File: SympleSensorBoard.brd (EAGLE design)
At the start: 50.8 x 50.8 mm, 49 parts, among them IC1 STM32F303K8T6, J1 B2B-XH-A_LF__SN_, J10 B3B-XH-A_LF__SN_, J11 B3B-XH-A_LF__SN_, J12 B4B-XH-A_LF__SN_, J13 B4B-XH-A_LF__SN_, J14 B4B-XH-A_LF__SN_, J15 B4B-XH-A_LF__SN_, J16 B2B-XH-A_LF__SN_, J2 B2B-XH-A_LF__SN_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

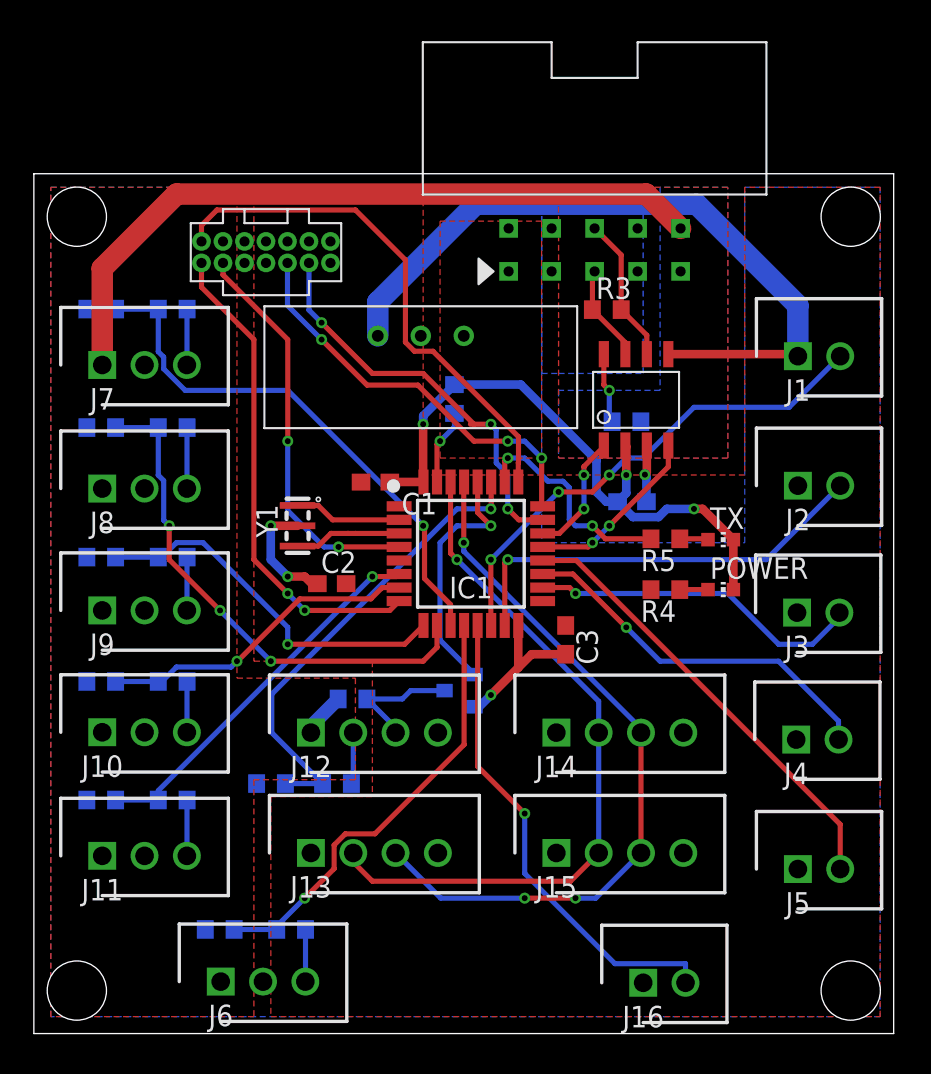
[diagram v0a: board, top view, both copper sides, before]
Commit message: コネクタ位置の修正、コネクタ番号を基盤上に表示、部品の再配置、再配線完了。使うセンサはまだ決まっていない。
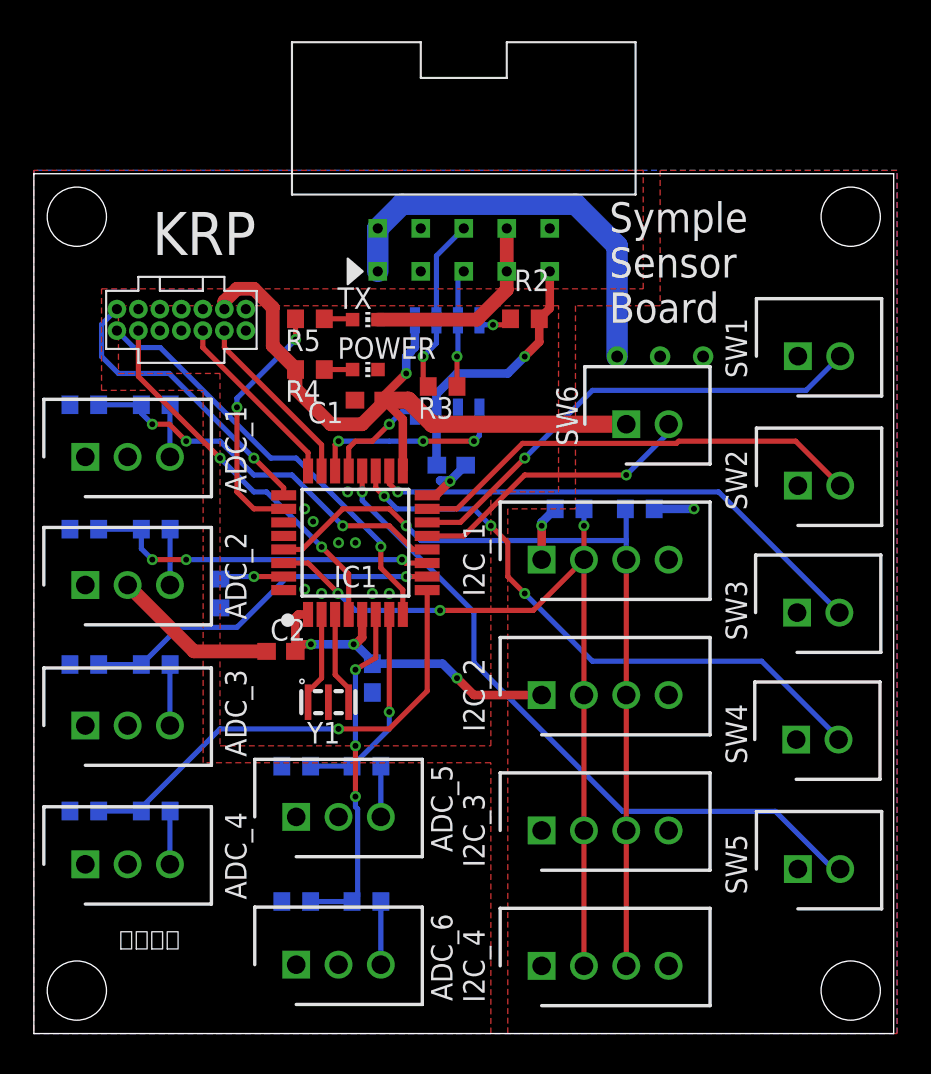
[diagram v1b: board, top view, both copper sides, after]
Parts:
- removed J10, J11, J6, J7, J8, J9: B3B-XH-A_LF__SN_, B3B-XH-A_LF__SN_:SHDR3W64P0X250_1X3_990X575X700
- removed J12, J13, J14, J15: B4B-XH-A_LF__SN_, B4B-XH-A_LF__SN_:SHDR4W64P0X250_1X4_1240X575X70
- removed J16: B2B-XH-A_LF__SN_, B2B-XH-A_LF__SN_:SHDR2W64P0X250_1X2_740X575X700
- removed MOSFET1: IRLML6344TRPBFTR, mukuchin_transistor_fet_igbt:IRLML6344TRPBF
- removed R18: 10k, rcl:R0603
- removed R19: 1k, rcl:R0603
- removed R20: 2k, rcl:R0603
- added ADC_1, ADC_2, ADC_3, ADC_4, ADC_5, ADC_6: B3B-XH-A_LF__SN_, B3B-XH-A_LF__SN_:SHDR3W64P0X250_1X3_990X575X700
- added I2C_1, I2C_2, I2C_3, I2C_4: B4B-XH-A_LF__SN_, B4B-XH-A_LF__SN_:SHDR4W64P0X250_1X4_1240X575X70
- added R21, R22: 10k, rcl:R0603
- added SW6: B2B-XH-A_LF__SN_, B2B-XH-A_LF__SN_:SHDR2W64P0X250_1X2_740X575X700
- moved R6 32.0 mm to (7.20, 37.1)
- moved R7 32.0 mm to (2.98, 37.1)
- moved R4 24.7 mm to (16.3, 39.2)
- moved R5 24.7 mm to (16.3, 42.2)
- moved POWER 24.7 mm to (19.6, 39.2)
- moved TX 24.7 mm to (19.6, 42.2)
- moved R1 18.0 mm to (11.0, 26.0), turned to 270 degrees
- moved R12 15.0 mm to (7.20, 13.2)
- moved R13 15.0 mm to (2.98, 13.2)
- moved U$1 14.2 mm to (37.0, 40.0), flipped to the bottom
- moved R10 14.0 mm to (7.20, 21.8)
- moved R11 14.0 mm to (2.98, 21.8)
- moved R8 13.0 mm to (7.20, 29.8)
- moved R9 13.0 mm to (2.98, 29.8)
- moved R17 13.0 mm to (15.5, 7.80)
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- renumbered J1 to SW1, J2 to SW2, J3 to SW3, J4 to SW4, J5 to SW5
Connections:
- removed net ECHO: IC1.28, MOSFET1.P$1
- removed net N$11: J12.3, MOSFET1.P$3, R18.1
- removed net N$13: J12.2, R19.1
- removed net TRIG: IC1.27, R19.2, R20.2
- net +3.3V: now also I2C_1.1, I2C_2.1, I2C_3.1, I2C_4.1, R21.1, R22.1, SW6.1; no longer J13.1, J14.1, J15.1, J16.1
- net +5V: now also ADC_1.1, ADC_2.1, ADC_3.1, ADC_4.1, ADC_5.1, ADC_6.1; no longer J10.1, J11.1, J12.1, J6.1, J7.1, J8.1, J9.1, R18.2
- net GND: now also ADC_1.2, ADC_2.2, ADC_3.2, ADC_4.2, ADC_5.2, ADC_6.2, I2C_1.4, I2C_2.4, I2C_3.4, I2C_4.4; no longer J10.2, J11.2, J12.4, J13.4, J14.4, J15.4, J6.2, J7.2, J8.2, J9.2, MOSFET1.P$2, R20.1
- net MSW6: now also SW6.2; no longer J16.2
- net N$10: now also ADC_6.3; no longer J11.3
- net N$5: now also ADC_1.3; no longer J6.3
- net N$6: now also ADC_2.3; no longer J7.3
- net N$7: now also ADC_3.3; no longer J8.3
- net N$8: now also ADC_4.3; no longer J9.3
- net N$9: now also ADC_5.3; no longer J10.3
- net SCL: now also I2C_1.3, I2C_2.3, I2C_3.3, I2C_4.3, R21.2; no longer J13.3, J14.3, J15.3
- net SDA: now also I2C_1.2, I2C_2.2, I2C_3.2, I2C_4.2, R22.2; no longer J13.2, J14.2, J15.2
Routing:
- net +5V: track 48.6 -> 16.0 mm
- net TRIG: track 27.8 -> 0.00 mm, vias 1 -> 0
- net GND: track 52.9 -> 26.0 mm, vias 6 -> 1
- net +3.3V: track 42.4 -> 67.8 mm, vias 0 -> 6
- net +12V: track 0.00 -> 24.8 mm
- net ECHO: track 15.0 -> 0.00 mm, vias 1 -> 0
- net MSW5: track 26.7 -> 40.7 mm, vias 0 -> 1
- net SWDIO: track 24.3 -> 10.7 mm, vias 3 -> 0
- net MSW4: track 22.2 -> 35.7 mm, vias 1 -> 3
- net VCP_RX: track 31.1 -> 17.6 mm, vias 0 -> 1
- net SWCLK: track 24.1 -> 10.9 mm, vias 3 -> 0
- net MSW6: track 28.6 -> 17.3 mm
- net AD2: track 31.9 -> 20.9 mm, vias 1 -> 3
- net MSW3: track 19.9 -> 30.5 mm
- net AD3: track 30.5 -> 21.6 mm, vias 3 -> 1
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- added copper zone on layer 1, net GND
- removed copper zone on layer 1, net +12V
- removed copper zone on layer 16, net +5V
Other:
- board text added: "KRP"
- board text added: "Symple Sensor Board"
- board text added: "向野晴登"

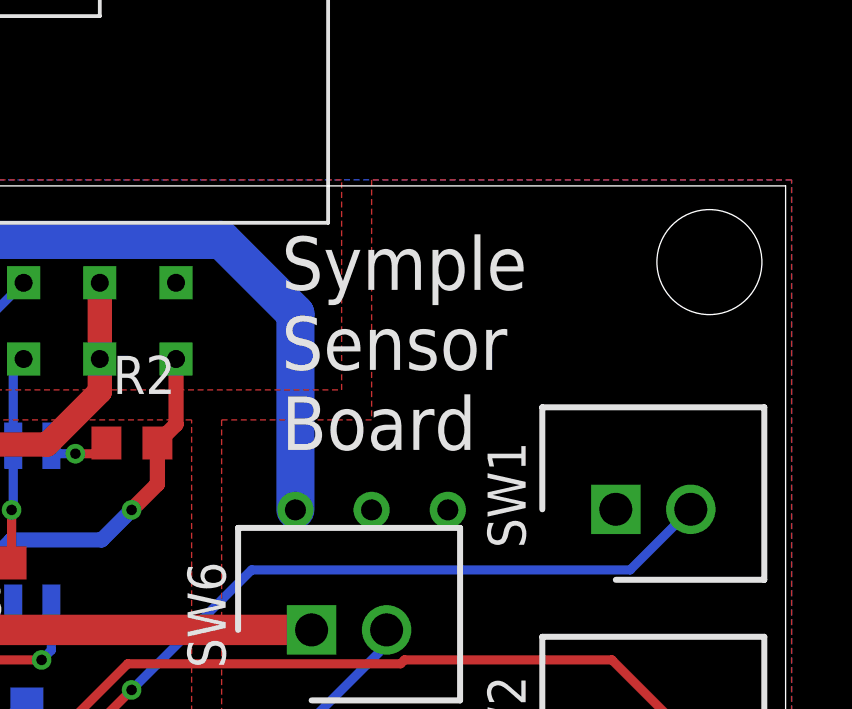
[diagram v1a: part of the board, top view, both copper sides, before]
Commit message: コネクタ位置の修正、コネクタ番号を基盤上に表示、部品の再配置、再配線完了。使うセンサはまだ決まっていない。
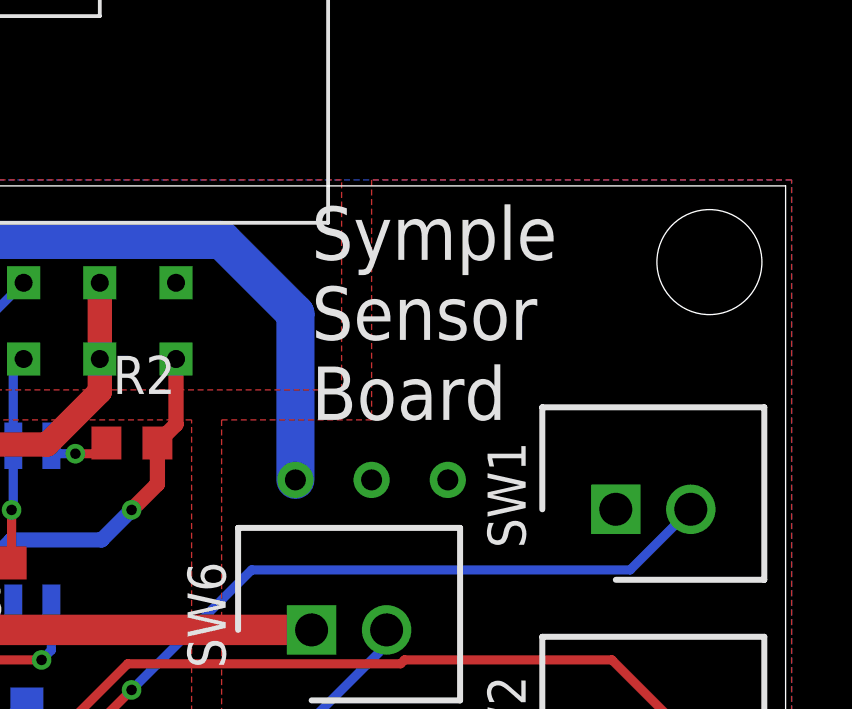
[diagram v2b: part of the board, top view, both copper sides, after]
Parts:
- moved U$1 1.00 mm to (37.0, 41.0)
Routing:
- net +12V: track 24.8 -> 23.8 mm
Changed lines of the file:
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@@
 <hole x="2.54" y="48.26" drill="3.5"/>
 <text x="7" y="46" size="2.54" layer="25">KRP</text>
-<text x="34" y="42" size="1.778" layer="25">Symple
+<text x="35" y="43" size="1.778" layer="25">Symple
 Sensor
 Board</text>
@@
 <attribute name="VALUE" x="31.015" y="32.905" size="1.27" layer="28" rot="MR180"/>
 </element>
-<element name="U$1" library="SympleEncoderBoard" package="DC/DC_REGULATOR_3P" value="BP5293-33" x="37" y="40" smashed="yes" rot="MR180"/>
+<element name="U$1" library="SympleEncoderBoard" package="DC/DC_REGULATOR_3P" value="BP5293-33" x="37" y="41" smashed="yes" rot="MR180"/>
 </elements>
 <signals>
@@
 <wire x1="21.75" y1="49" x2="32" y2="49" width="1.27" layer="16"/>
 <wire x1="32" y1="49" x2="34.46" y2="46.54" width="1.27" layer="16"/>
-<wire x1="34.46" y1="46.54" x2="34.46" y2="40" width="1.27" layer="16"/>
+<wire x1="34.46" y1="46.54" x2="34.46" y2="41" width="1.27" layer="16"/>
 </signal>
 <signal name="+5V">

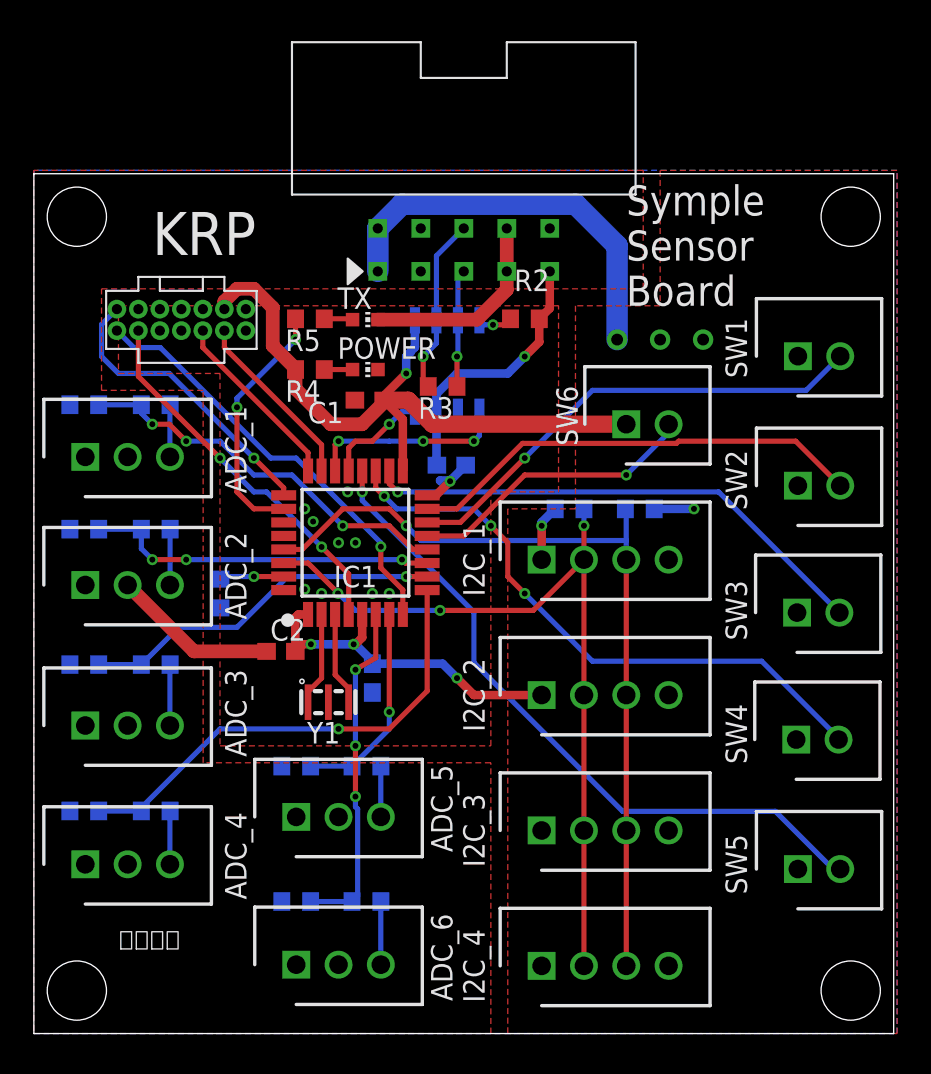
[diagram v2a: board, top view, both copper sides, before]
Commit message: I2Cコネクタを全て外した。I2Cは別の基盤で行う。
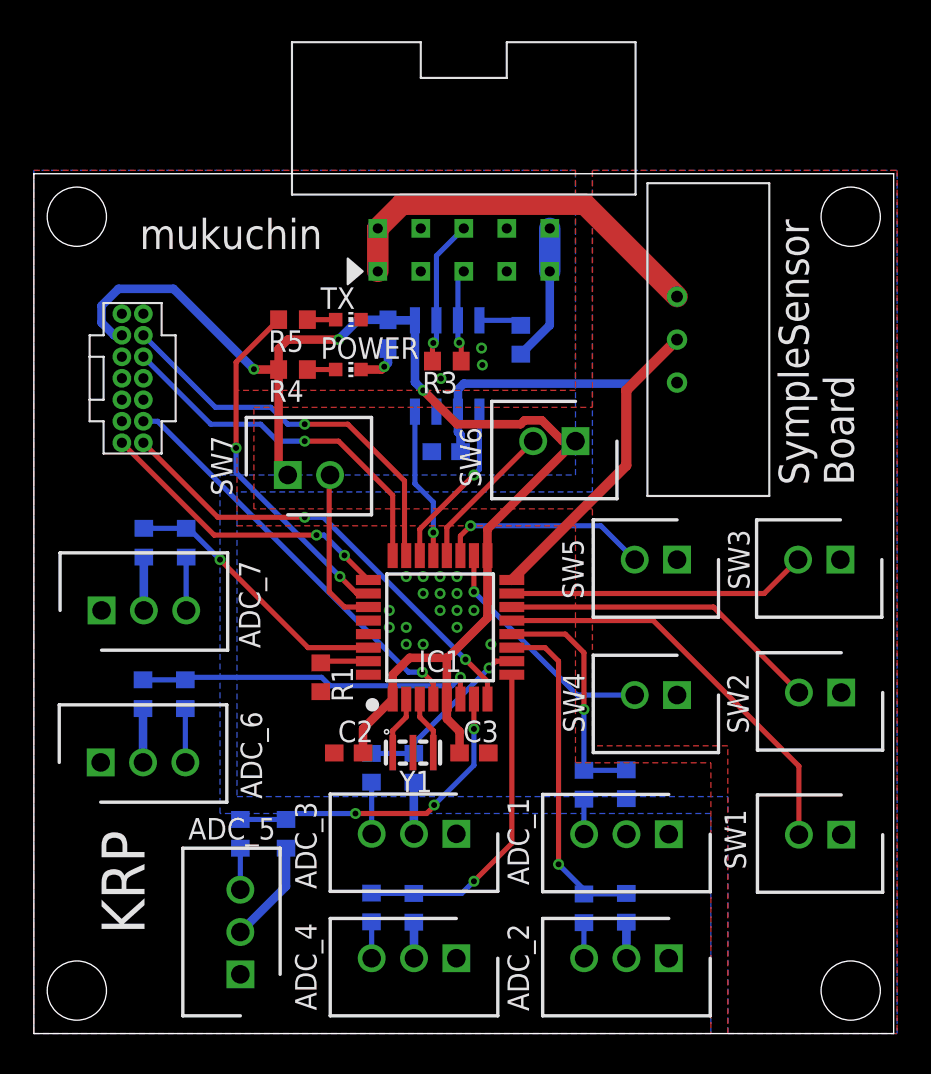
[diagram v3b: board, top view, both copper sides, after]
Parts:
- removed I2C_1, I2C_2, I2C_3, I2C_4: B4B-XH-A_LF__SN_, B4B-XH-A_LF__SN_:SHDR4W64P0X250_1X4_1240X575X70
- removed R21, R22: 10k, rcl:R0603
- added ADC_7: B3B-XH-A_LF__SN_, B3B-XH-A_LF__SN_:SHDR3W64P0X250_1X3_990X575X700
- added R18: 1k, rcl:R0603
- added R19: 2k, rcl:R0603
- added SW7: B2B-XH-A_LF__SN_, B2B-XH-A_LF__SN_:SHDR2W64P0X250_1X2_740X575X700
- moved ADC_1 41.0 mm to (37.5, 11.8), turned to 180 degrees
- moved ADC_2 40.9 mm to (37.5, 4.45), turned to 180 degrees
- moved R7 39.1 mm to (35.0, 14.7), turned to 90 degrees
- moved R9 39.1 mm to (35.0, 7.43), turned to 90 degrees
- moved R6 33.8 mm to (32.5, 14.7), turned to 270 degrees
- moved R8 33.8 mm to (32.5, 7.40), turned to 270 degrees
- moved SW1 28.4 mm to (47.7, 11.8), turned to 180 degrees
- moved ADC_3 22.8 mm to (25.0, 11.8), turned to 180 degrees
- moved ADC_4 22.6 mm to (25.0, 4.45), turned to 180 degrees
- moved R11 20.4 mm to (22.4, 15.7), turned to 90 degrees
- moved R13 20.3 mm to (22.4, 7.43), turned to 90 degrees
- moved SW5 19.6 mm to (38.0, 28.0), turned to 180 degrees
- moved ADC_6 16.6 mm to (3.95, 16.0)
- moved R16 16.3 mm to (8.95, 20.1), turned to 270 degrees
- moved R17 15.2 mm to (6.45, 20.1), turned to 90 degrees
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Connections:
- removed net SCL: I2C_1.3, I2C_2.3, I2C_3.3, I2C_4.3, IC1.29, R21.2
- removed net SDA: I2C_1.2, I2C_2.2, I2C_3.2, I2C_4.2, IC1.30, R22.2
- new net AD7: IC1.30, R18.1, R19.2
- new net MSW7: IC1.27, SW7.2
- new net N$20: ADC_7.3, R18.2
- net +3.3V: now also SW7.1; no longer I2C_1.1, I2C_2.1, I2C_3.1, I2C_4.1, R21.1, R22.1
- net +5V: now also ADC_7.1
- net GND: now also ADC_7.2, R19.1; no longer I2C_1.4, I2C_2.4, I2C_3.4, I2C_4.4
- net MSW1: now also IC1.13; no longer IC1.14
- net MSW2: now also IC1.14; no longer IC1.15
- net MSW3: now also IC1.15; no longer IC1.18
- net MSW4: now also IC1.18; no longer IC1.19
- net MSW5: now also IC1.19; no longer IC1.20
- net MSW6: now also IC1.20; no longer IC1.13
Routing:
- net SCL: track 49.0 -> 0.00 mm, vias 1 -> 0
- net SDA: track 47.2 -> 0.00 mm, vias 3 -> 0
- net GND: track 26.0 -> 58.5 mm
- net MSW5: track 40.7 -> 12.5 mm
- net MSW4: track 35.7 -> 14.2 mm, vias 3 -> 1
- net AD7: track 0.00 -> 16.2 mm, vias 0 -> 1
- net SWDIO: track 10.7 -> 23.4 mm, vias 0 -> 1
- net MSW3: track 30.5 -> 17.7 mm, vias 1 -> 0
- net SWCLK: track 10.9 -> 21.7 mm, vias 0 -> 1
- net AD3: track 21.6 -> 10.9 mm
- net +3.3V: track 67.8 -> 77.5 mm, vias 6 -> 3
- net MSW7: track 0.00 -> 9.61 mm
- net AD1: track 23.2 -> 14.2 mm, vias 3 -> 1
- net AD4: track 28.4 -> 19.5 mm
- net MSW6: track 17.3 -> 8.87 mm, vias 1 -> 0
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- added copper zone on layer 16, net +5V
- removed copper zone on layer 1, net +5V
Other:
- board text added: "SympleSensor Board"
- board text added: "mukuchin"
- board text removed: "Symple Sensor Board"
- board text removed: "向野晴登"
